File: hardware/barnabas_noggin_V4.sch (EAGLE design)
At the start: 59 parts, among them J1 POWER_JACKPTH, J10 2.54mm, J2 ICSP, J3 ICSP, J4 USB-mini-90 -SMD, J5 ICSP, J6 2.54mm, J7 2.54mm, J8 2.54mm, J9 2.54mm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

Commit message: Replaced with new ATMEGA328 chip and modified PWM pins
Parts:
- U2: value ATMEGA328P-32MUR -> ATMEGA328P-AU; device barnabas_noggin_V4:ATMEGA328P-32MUR -> barnabas_noggin_V4:ATMEGA328P-32AU; PARTNO ATMEGA328P-MUR -> ATMEGA328P-AU
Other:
- moved on the sheet: U2
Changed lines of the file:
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@@
 <attribute name="PARTNO" value="LTST-C171KSKT"/>
 </part>
-<part name="U2" library="barnabas_noggin_V4" deviceset="ATMEGA328P-32" device="MUR" value="ATMEGA328P-32MUR">
-<attribute name="PARTNO" value="ATMEGA328P-MUR"/>
+<part name="U2" library="barnabas_noggin_V4" deviceset="ATMEGA328P-32" device="AU" value="ATMEGA328P-AU">
+<attribute name="PARTNO" value="ATMEGA328P-AU"/>
 </part>
 <part name="U$52" library="barnabas_noggin_V4" deviceset="GND" device=""/>

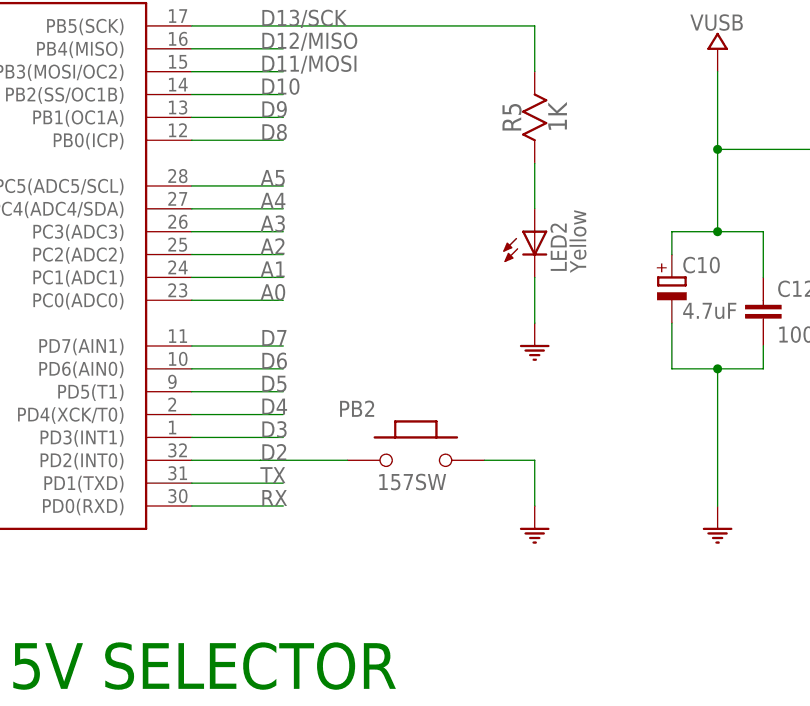
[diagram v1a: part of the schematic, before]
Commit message: Replaced fuses. Added pull-up resistor for pin 2.
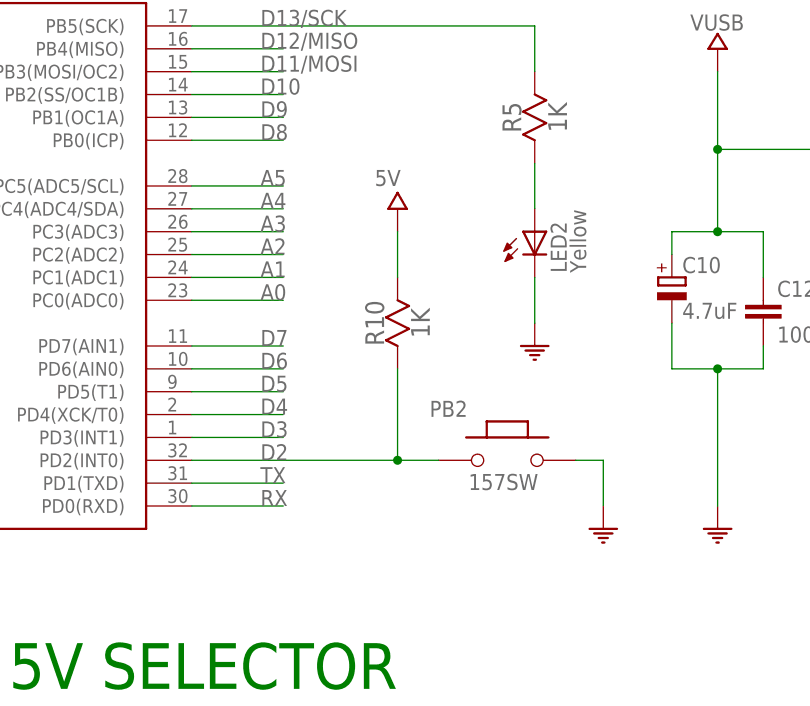
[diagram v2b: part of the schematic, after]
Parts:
- added R10: 1K, barnabas_noggin_V4:RESISTOR0603
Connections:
- net 5V: now also R10.2
- net D2: now also R10.1
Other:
- moved on the sheet: PB2
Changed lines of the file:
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@@
 <attribute name="PARTNO" value="MF-FSMF050X-2"/>
 </part>
+<part name="R10" library="barnabas_noggin_V4" deviceset="RESISTOR" device="0603" value="1K">
+<attribute name="PARTNO" value="RC0603FR-071KL "/>
+</part>
+<part name="U$46" library="barnabas_noggin_V4" deviceset="5V" device=""/>
 </parts>
 <sheets>
@@
 <attribute name="PARTNO" x="100.584" y="73.66" size="1.778" layer="96" display="off"/>
 </instance>
-<instance part="PB2" gate="G$1" x="134.112" y="121.92">
-<attribute name="PARTNO" x="134.112" y="121.92" size="1.778" layer="96" display="off"/>
-</instance>
-<instance part="U$40" gate="G$1" x="147.32" y="114.3"/>
+<instance part="PB2" gate="G$1" x="144.272" y="121.92">
+<attribute name="PARTNO" x="144.272" y="121.92" size="1.778" layer="96" display="off"/>
+</instance>
+<instance part="U$40" gate="G$1" x="154.94" y="114.3"/>
 <instance part="J6" gate="A" x="284.48" y="72.39">
 <attribute name="PARTNO" x="284.48" y="72.39" size="1.778" layer="96" display="off"/>
@@
 <attribute name="PARTNO" x="236.22" y="81.28" size="1.778" layer="96" rot="R90" display="off"/>
 </instance>
+<instance part="R10" gate="G$1" x="132.08" y="137.16" rot="R90">
+<attribute name="PARTNO" x="132.08" y="137.16" size="1.778" layer="96" rot="R90" display="off"/>
+</instance>
+<instance part="U$46" gate="G$1" x="132.08" y="149.86"/>
 </instances>
 <busses>
@@
 <segment>
 <pinref part="U2" gate="G$1" pin="PD2(INT0)"/>
-<wire x1="109.22" y1="121.92" x2="116.84" y2="121.92" width="0.1524" layer="91"/>
 <label x="116.84" y="121.92" size="1.778" layer="95"/>
+<pinref part="R10" gate="G$1" pin="1"/>
+<wire x1="132.08" y1="132.08" x2="132.08" y2="121.92" width="0.1524" layer="91"/>
+<wire x1="132.08" y1="121.92" x2="109.22" y2="121.92" width="0.1524" layer="91"/>
 <pinref part="PB2" gate="G$1" pin="1"/>
-<wire x1="116.84" y1="121.92" x2="119.38" y2="121.92" width="0.1524" layer="91"/>
-<wire x1="126.492" y1="121.92" x2="119.38" y2="121.92" width="0.1524" layer="91"/>
+<wire x1="136.652" y1="121.92" x2="132.08" y2="121.92" width="0.1524" layer="91"/>
+<junction x="132.08" y="121.92"/>
 </segment>
 <segment>
@@
 </segment>
 <segment>
-<pinref part="PB2" gate="G$1" pin="2"/>
-<pinref part="U$40" gate="G$1" pin="GND"/>
-<wire x1="141.732" y1="121.92" x2="147.32" y2="121.92" width="0.1524" layer="91"/>
-<wire x1="147.32" y1="121.92" x2="147.32" y2="116.84" width="0.1524" layer="91"/>
-</segment>
-<segment>
 <pinref part="U$41" gate="G$1" pin="GND"/>
 <wire x1="264.16" y1="66.04" x2="264.16" y2="72.39" width="0.1524" layer="91"/>
@@
 <pinref part="U$45" gate="G$1" pin="GND"/>
 <wire x1="226.06" y1="69.85" x2="226.06" y2="66.04" width="0.1524" layer="91"/>
+</segment>
+<segment>
+<pinref part="U$40" gate="G$1" pin="GND"/>
+<pinref part="PB2" gate="G$1" pin="2"/>
+<wire x1="154.94" y1="116.84" x2="154.94" y2="121.92" width="0.1524" layer="91"/>
+<wire x1="154.94" y1="121.92" x2="151.892" y2="121.92" width="0.1524" layer="91"/>
 </segment>
 </net>
@@
 <junction x="192.024" y="81.28"/>
 </segment>
-</net>
+<segment>
+<pinref part="U$46" gate="G$1" pin="5V"/>
+<pinref part="R10" gate="G$1" pin="2"/>
+<wire x1="132.08" y1="147.32" x2="132.08" y2="142.24" width="0.1524" layer="91"/>
+</segment>
+</net>

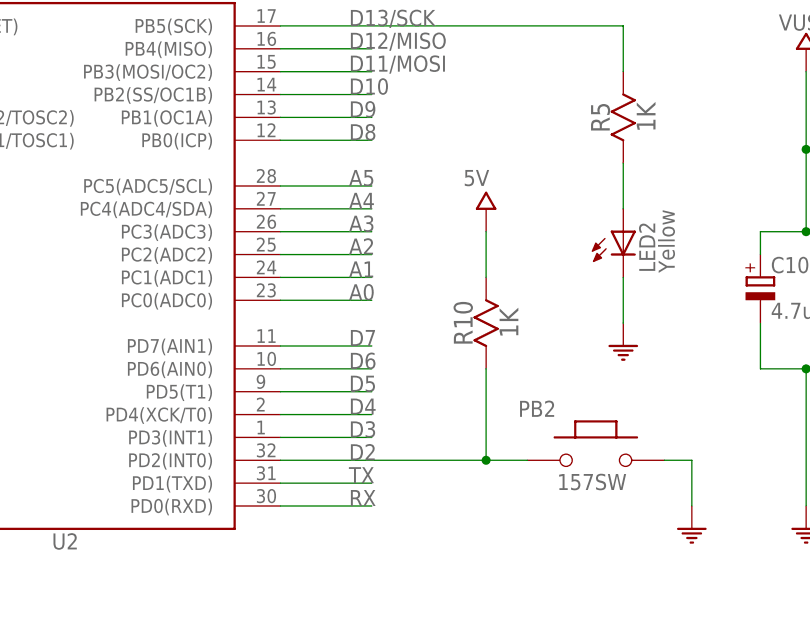
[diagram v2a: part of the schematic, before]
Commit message: Removed pin2 pullup resistor. Uploaded and updated files for Rev3B.
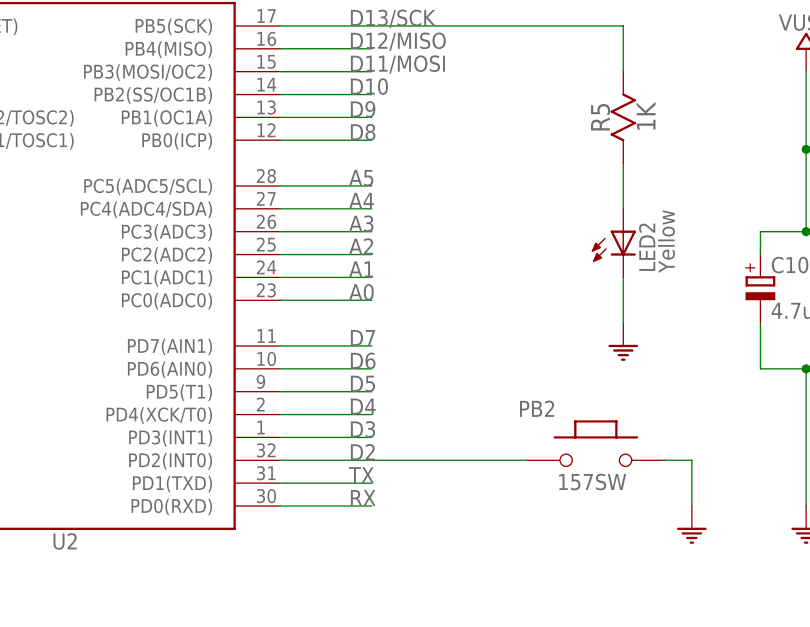
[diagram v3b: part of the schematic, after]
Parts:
- removed R10: 1K, barnabas_noggin_V4:RESISTOR0603
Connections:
- net 5V: no longer R10.2
- net D2: no longer R10.1
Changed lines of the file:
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@@
 <attribute name="PARTNO" value="MF-FSMF050X-2"/>
 </part>
-<part name="R10" library="barnabas_noggin_V4" deviceset="RESISTOR" device="0603" value="1K">
-<attribute name="PARTNO" value="RC0603FR-071KL "/>
-</part>
-<part name="U$46" library="barnabas_noggin_V4" deviceset="5V" device=""/>
 </parts>
 <sheets>
@@
 <attribute name="PARTNO" x="236.22" y="81.28" size="1.778" layer="96" rot="R90" display="off"/>
 </instance>
-<instance part="R10" gate="G$1" x="132.08" y="137.16" rot="R90">
-<attribute name="PARTNO" x="132.08" y="137.16" size="1.778" layer="96" rot="R90" display="off"/>
-</instance>
-<instance part="U$46" gate="G$1" x="132.08" y="149.86"/>
 </instances>
 <busses>
@@
 <pinref part="U2" gate="G$1" pin="PD2(INT0)"/>
 <label x="116.84" y="121.92" size="1.778" layer="95"/>
-<pinref part="R10" gate="G$1" pin="1"/>
-<wire x1="132.08" y1="132.08" x2="132.08" y2="121.92" width="0.1524" layer="91"/>
-<wire x1="132.08" y1="121.92" x2="109.22" y2="121.92" width="0.1524" layer="91"/>
+<wire x1="136.652" y1="121.92" x2="109.22" y2="121.92" width="0.1524" layer="91"/>
 <pinref part="PB2" gate="G$1" pin="1"/>
-<wire x1="136.652" y1="121.92" x2="132.08" y2="121.92" width="0.1524" layer="91"/>
-<junction x="132.08" y="121.92"/>
 </segment>
 <segment>
@@
 <junction x="192.024" y="81.28"/>
 </segment>
-<segment>
-<pinref part="U$46" gate="G$1" pin="5V"/>
-<pinref part="R10" gate="G$1" pin="2"/>
-<wire x1="132.08" y1="147.32" x2="132.08" y2="142.24" width="0.1524" layer="91"/>
-</segment>
-</net>
+</net>
